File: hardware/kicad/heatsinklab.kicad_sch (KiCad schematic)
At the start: 18 parts, among them J1 PWR_IN 12V JST-XH 2p, J10 EXT1 Future Airspeed JST-XH 4p, J2 HEATER_OUT JST-XH 2p, J4 FAN_OUT JST-XH 2p, J5 FAN_PWM GPIO5 JST-XH 2p, J6 THERMO MAX6675 SPI JST-XH 5p, J7 INA226 I2C 0x41 JST-XH 4p, J8 SDP510 I2C 0x40 JST-XH 4p, J9 EZO-HUM I2C 0x6F JST-XH 4p, Q1 IRLZ44N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

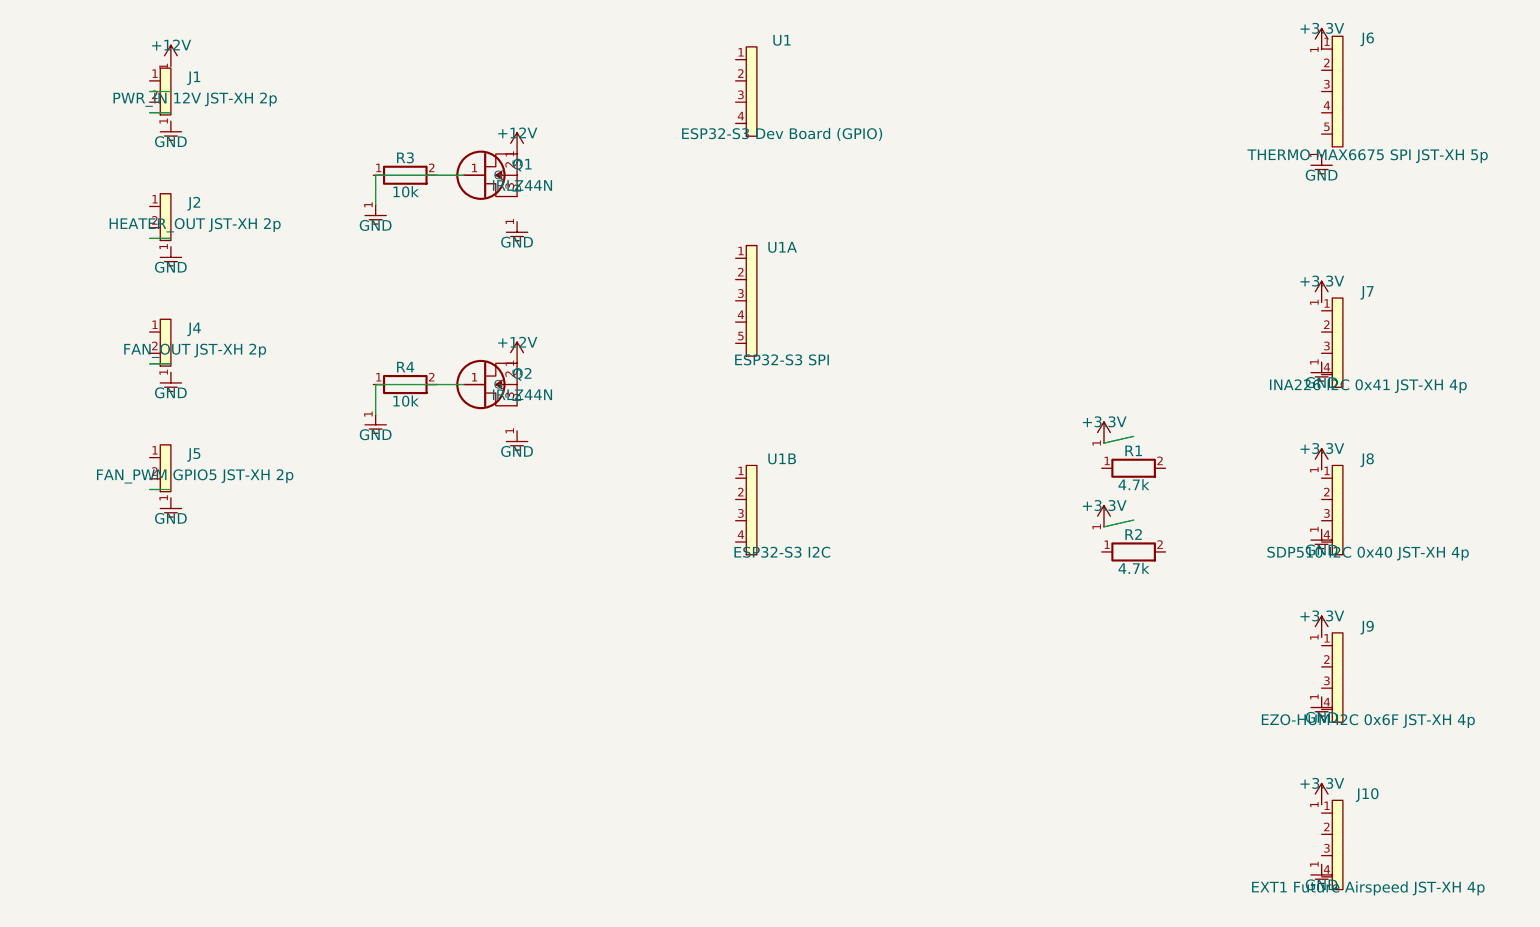
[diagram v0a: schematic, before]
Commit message: Rewrite KiCad schematic with correct KiCad 9 s-expression syntax
Fix net_label->label, remove invalid property inside labels, fix
fields_autoplaced, use proper UUIDs, correct all symbol definitions.

https://claude.ai/code/session_01WnNzHJgAA7wxew4mtPpYTu
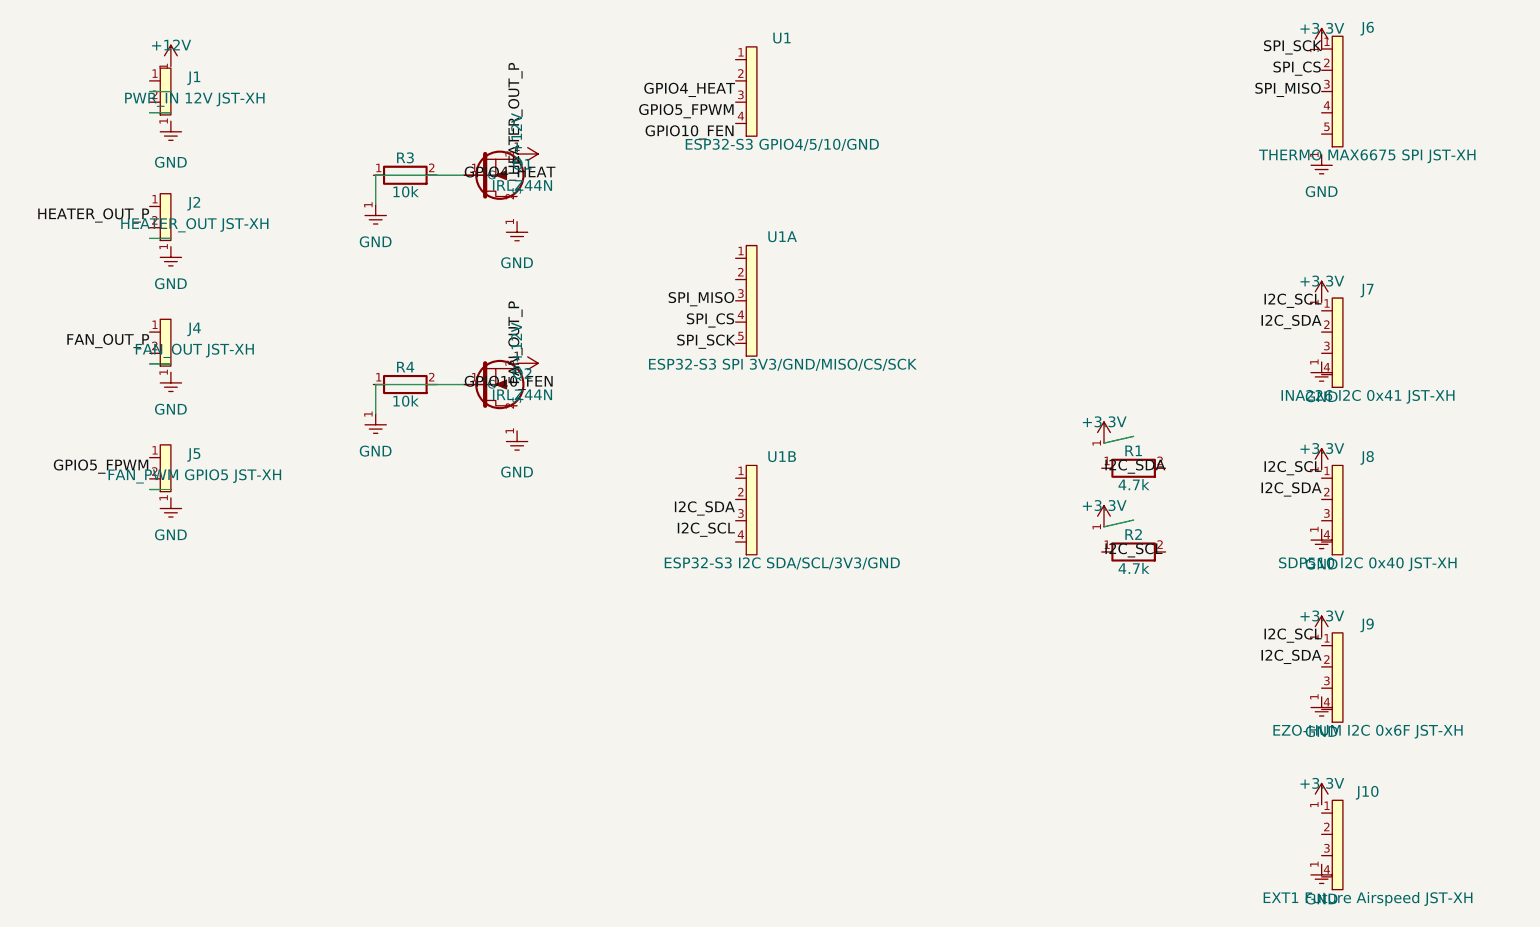
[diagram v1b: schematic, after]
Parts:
- removed Q1, Q2: IRLZ44N, Package_TO_SOT_THT:TO-220-3_Vertical, symbol Device:IRLZ44N
- added Q1, Q2: IRLZ44N, Package_TO_SOT_THT:TO-220-3_Vertical, symbol Device:Q_NMOS_GDS
- J1: value PWR_IN 12V JST-XH 2p -> PWR_IN 12V JST-XH
- J10: value EXT1 Future Airspeed JST-XH 4p -> EXT1 Future Airspeed JST-XH
- J2: value HEATER_OUT JST-XH 2p -> HEATER_OUT JST-XH
- J4: value FAN_OUT JST-XH 2p -> FAN_OUT JST-XH
- J5: value FAN_PWM GPIO5 JST-XH 2p -> FAN_PWM GPIO5 JST-XH
- J6: value THERMO MAX6675 SPI JST-XH 5p -> THERMO MAX6675 SPI JST-XH
- J7: value INA226 I2C 0x41 JST-XH 4p -> INA226 I2C 0x41 JST-XH
- J8: value SDP510 I2C 0x40 JST-XH 4p -> SDP510 I2C 0x40 JST-XH
- J9: value EZO-HUM I2C 0x6F JST-XH 4p -> EZO-HUM I2C 0x6F JST-XH
- U1: value ESP32-S3 Dev Board (GPIO) -> ESP32-S3 GPIO4/5/10/GND
- U1A: value ESP32-S3 SPI -> ESP32-S3 SPI 3V3/GND/MISO/CS/SCK
- U1B: value ESP32-S3 I2C -> ESP32-S3 I2C SDA/SCL/3V3/GND
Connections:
- net SPI_SCK: now reaches J6.1 (Pin_1)
- net SPI_CS: now reaches J6.2 (Pin_2)
- net SPI_MISO: now reaches J6.3 (Pin_3)
- new net GPIO10_FEN: Q2.1 (G)
- new net GPIO4_HEAT: Q1.1 (G)
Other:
- title: HeatsinkLab Wind Tunnel — Carrier Board -> HeatsinkLab Wind Tunnel Carrier Board

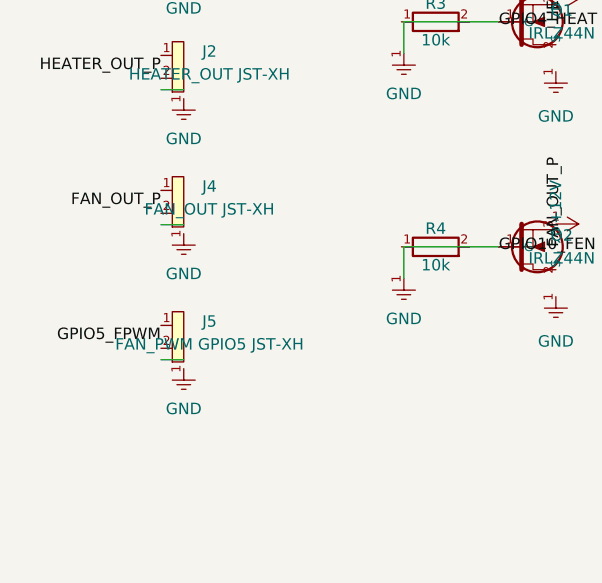
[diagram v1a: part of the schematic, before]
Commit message: Merge FAN_OUT + FAN_PWM into single 3-pin JST-XH connector J4
J4 now carries: pin1=12V(via Q2), pin2=GND, pin3=GPIO5_PWM.
Removes separate J5 2-pin connector. Adds Conn_01x03 lib symbol.
Updates PCB footprint to JST_XH_B3B-XH-A and wiring schematic doc.

https://claude.ai/code/session_01WnNzHJgAA7wxew4mtPpYTu
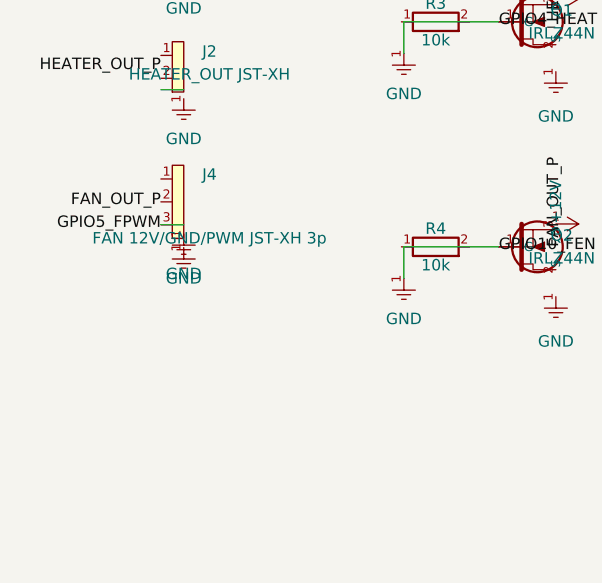
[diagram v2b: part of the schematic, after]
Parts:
- removed J5: FAN_PWM GPIO5 JST-XH, Connector_JST:JST_XH_B2B-XH-A_1x02_P2.50mm_Vertical, symbol Connector_Generic:Conn_01x02
- J4: value FAN_OUT JST-XH -> FAN 12V/GND/PWM JST-XH 3p; footprint Connector_JST:JST_XH_B2B-XH-A_1x02_P2.50mm_Vertical -> Connector_JST:JST_XH_B3B-XH-A_1x03_P2.50mm_Vertical; symbol Connector_Generic:Conn_01x02 -> Connector_Generic:Conn_01x03
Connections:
- net FAN_OUT_P: now also J4.2 (Pin_2)
- net GPIO5_FPWM: now also J4.3 (Pin_3)
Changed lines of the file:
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@@
     (pin "2")
   )
-  (symbol (lib_id "Connector_Generic:Conn_01x02") (at 20 50 0) (unit 1)
-    (exclude_from_sim no) (in_bom yes) (on_board yes)
-    (property "Reference" "J4" (at 22.86 48.288 0)
-      (effects (font (size 1.27 1.27)))
-    )
-    (property "Value" "FAN_OUT JST-XH" (at 22.86 50.828 0)
-      (effects (font (size 1.27 1.27)))
-    )
-    (property "Footprint" "Connector_JST:JST_XH_B2B-XH-A_1x02_P2.50mm_Vertical" (at 0 0 0)
-      (effects (font (size 1.27 1.27)) hide)
-    )
-    (property "Datasheet" "~" (at 0 0 0)
-      (effects (font (size 1.27 1.27)) hide)
-    )
-    (pin "1")
-    (pin "2")
-  )
-  (symbol (lib_id "Connector_Generic:Conn_01x02") (at 20 65 0) (unit 1)
-    (exclude_from_sim no) (in_bom yes) (on_board yes)
-    (property "Reference" "J5" (at 22.86 63.288 0)
-      (effects (font (size 1.27 1.27)))
-    )
-    (property "Value" "FAN_PWM GPIO5 JST-XH" (at 22.86 65.828 0)
-      (effects (font (size 1.27 1.27)))
-    )
-    (property "Footprint" "Connector_JST:JST_XH_B2B-XH-A_1x02_P2.50mm_Vertical" (at 0 0 0)
-      (effects (font (size 1.27 1.27)) hide)
-    )
-    (property "Datasheet" "~" (at 0 0 0)
-      (effects (font (size 1.27 1.27)) hide)
-    )
-    (pin "1")
-    (pin "2")
+  (symbol (lib_id "Connector_Generic:Conn_01x03") (at 20 50 0) (unit 1)
+    (exclude_from_sim no) (in_bom yes) (on_board yes)
+    (property "Reference" "J4" (at 22.86 46.96 0)
+      (effects (font (size 1.27 1.27)))
+    )
+    (property "Value" "FAN 12V/GND/PWM JST-XH 3p" (at 22.86 54.04 0)
+      (effects (font (size 1.27 1.27)))
+    )
+    (property "Footprint" "Connector_JST:JST_XH_B3B-XH-A_1x03_P2.50mm_Vertical" (at 0 0 0)
+      (effects (font (size 1.27 1.27)) hide)
+    )
+    (property "Datasheet" "~" (at 0 0 0)
+      (effects (font (size 1.27 1.27)) hide)
+    )
+    (pin "1")
+    (pin "2")
+    (pin "3")
   )
   (symbol (lib_id "Connector_Generic:Conn_01x05") (at 160 20 0) (unit 1)
@@
     (pin "1")
   )
-  (symbol (lib_id "power:GND") (at 20 68.54 0) (unit 1)
+  (symbol (lib_id "power:GND") (at 20 55.08 0) (unit 1)
     (exclude_from_sim no) (in_bom yes) (on_board yes)
     (property "Reference" "#PWR09" (at 0 0 0) (effects (font (size 1.27 1.27)) hide))
-    (property "Value" "GND" (at 20 73 0) (effects (font (size 1.27 1.27))))
+    (property "Value" "GND" (at 20 58.5 0) (effects (font (size 1.27 1.27))))
     (property "Footprint" "" (at 0 0 0) (effects (font (size 1.27 1.27)) hide))
     (property "Datasheet" "" (at 0 0 0) (effects (font (size 1.27 1.27)) hide))
@@
     (effects (font (size 1.27 1.27)) (justify right))
   )
-  (label "GPIO5_FPWM" (at 17.46 65 180)
+  (label "GPIO5_FPWM" (at 17.46 52.54 180)
     (effects (font (size 1.27 1.27)) (justify right))
   )
@@
   (wire (pts (xy 17.46 52.54) (xy 20 52.54))
   )
-  (wire (pts (xy 17.46 67.54) (xy 20 67.54))
-  )
   (wire (pts (xy 131.46 62) (xy 135 61.19))
